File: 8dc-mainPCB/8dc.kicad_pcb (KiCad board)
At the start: 2 copper layers, 41 x 116 mm, 60 parts, among them J1 PJ301M-12, J10 PJ301M-12, J11 PJ301M-12, J2 PJ301M-12, J3 PJ301M-12, J4 PJ301M-12, J5 PJ301M-12, J6 PJ301M-12, J7 PJ301M-12, J8 PJ301M-12, J9 EURO_PWR_2x5, U1 ADC0820, U2 TL064, U3 TL064, U4 L7805

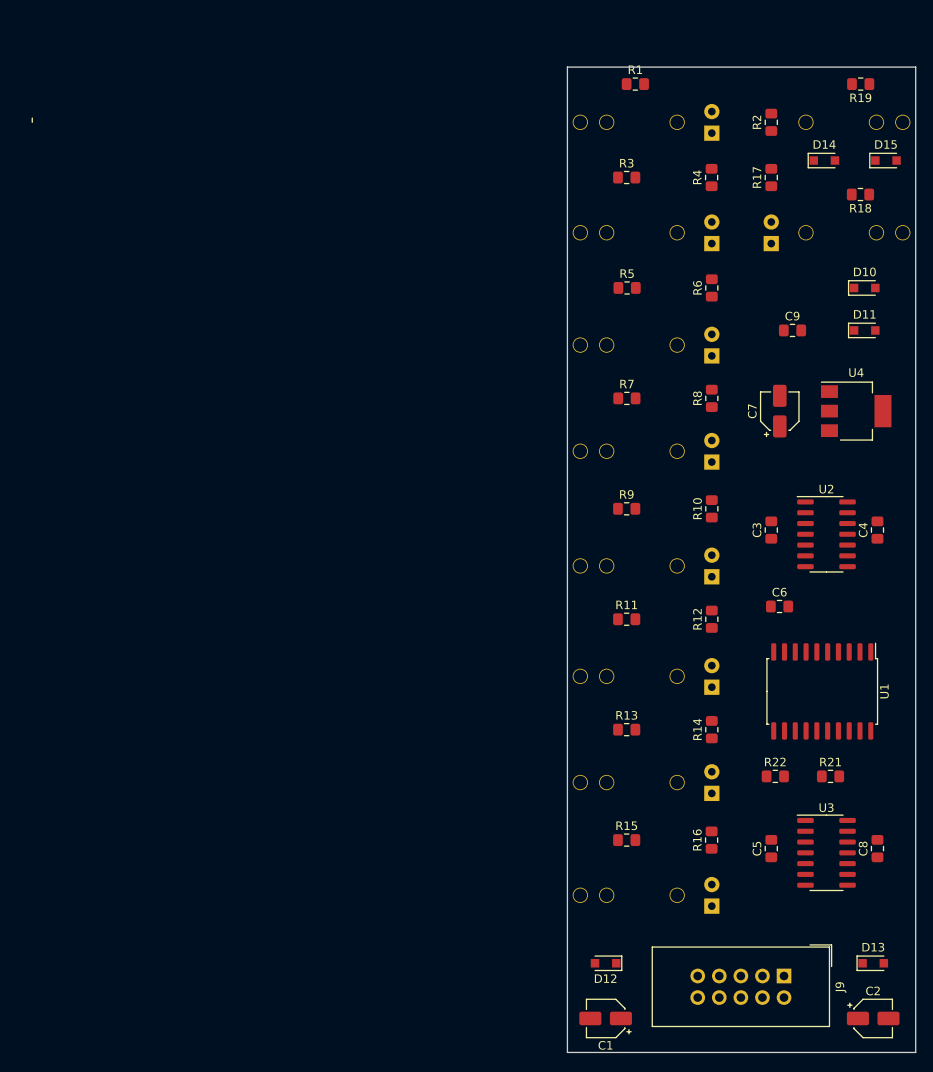
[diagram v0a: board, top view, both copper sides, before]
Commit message: Subdirectories, and fix power header
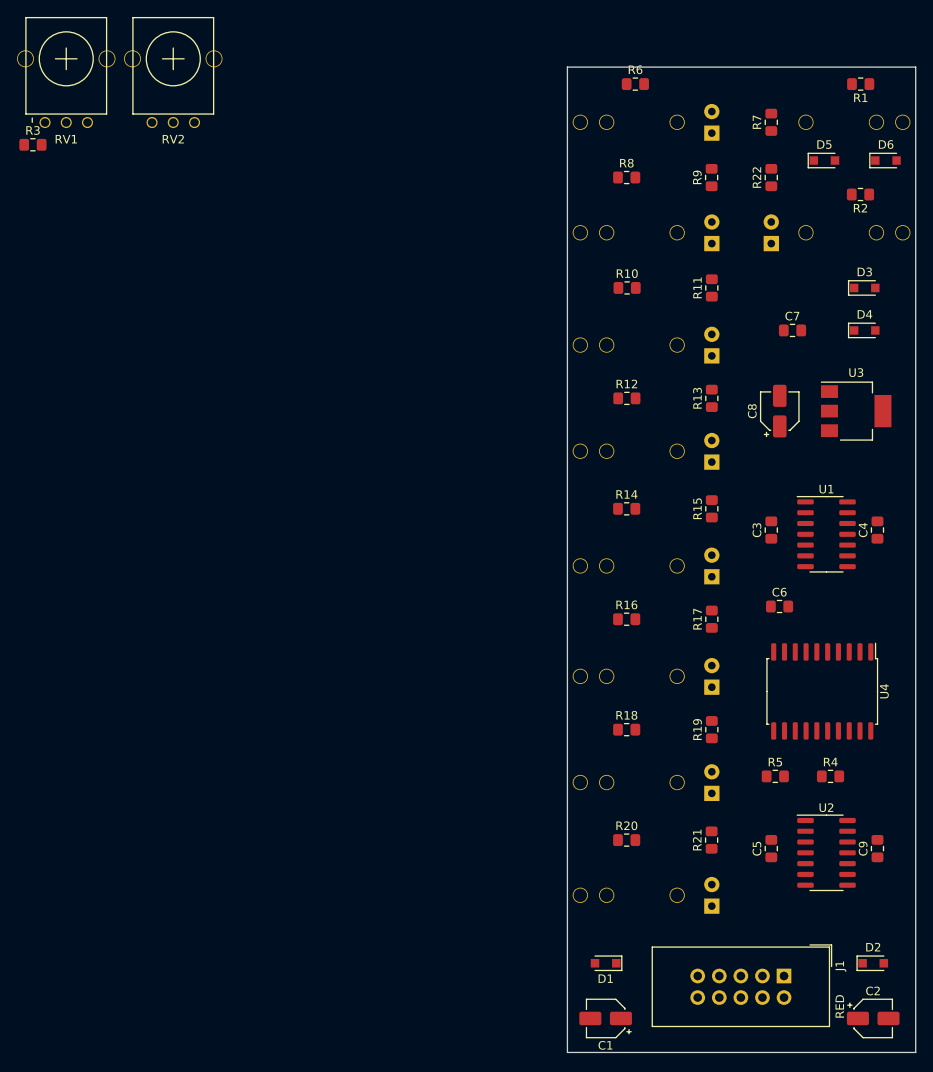
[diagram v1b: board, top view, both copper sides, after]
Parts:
- added R3: 100K, Resistor_SMD:R_0805_2012Metric_Pad1.15x1.40mm_HandSolder, F.Cu at (136.1, 39.1)
- added RV1: 100k, Eurocad:Alpha9mmPot, F.Cu at (140.0, 29.0)
- added RV2: 100k, Eurocad:Alpha9mmPot, F.Cu at (152.6, 29.0)
- J1: renamed from J9; footprint Connector_IDC:IDC-Header_2x05_P2.54mm_Vertical -> EurorackRSH:Eurorack_Power_Header_Shrouded
- R1: renamed from R19; value 1K -> 100K
- R2: renamed from R18; value 1K -> 100K
- renumbered C9 to C7, C7 to C8, C8 to C9, D12 to D1, D4 to D10, D5 to D11, D6 to D12, D7 to D13, D8 to D14, D9 to D15, D13 to D2, D10 to D3, D11 to D4, D14 to D5, D15 to D6, D1 to D7, D2 to D8, D3 to D9, J7 to J10, J8 to J11, J10 to J2, J11 to J3, J1 to J4, J2 to J5, J3 to J6, J4 to J7, J5 to J8, J6 to J9, R5 to R10, R6 to R11, R7 to R12, R8 to R13, R9 to R14, R10 to R15, R11 to R16, R12 to R17, R13 to R18, R14 to R19, R15 to R20, R16 to R21, R17 to R22, R21 to R4, R22 to R5, R1 to R6, R2 to R7, R3 to R8, R4 to R9, U2 to U1, U3 to U2, U4 to U3, U1 to U4
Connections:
- D1 pad 1: /+12V -> Net-(C1-Pad1)
- D1 pad 2: Net-(C1-Pad1) -> /+12V
- D2 pad 1: Net-(C2-Pad1) -> /-12V
- D2 pad 2: /-12V -> Net-(C2-Pad1)
- J1 pad 1: /+12V -> /-12V
- J1 pad 10: /-12V -> /+12V
- J1 pad 2: /+12V -> /-12V
- J1 pad 9: /-12V -> /+12V
- R2 pad 2: /CV_IN -> Net-(R2-Pad2)
